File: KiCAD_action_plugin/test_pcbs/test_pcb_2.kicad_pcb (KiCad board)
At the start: 2 copper layers, 36.6 x 26.5 mm, 6 parts

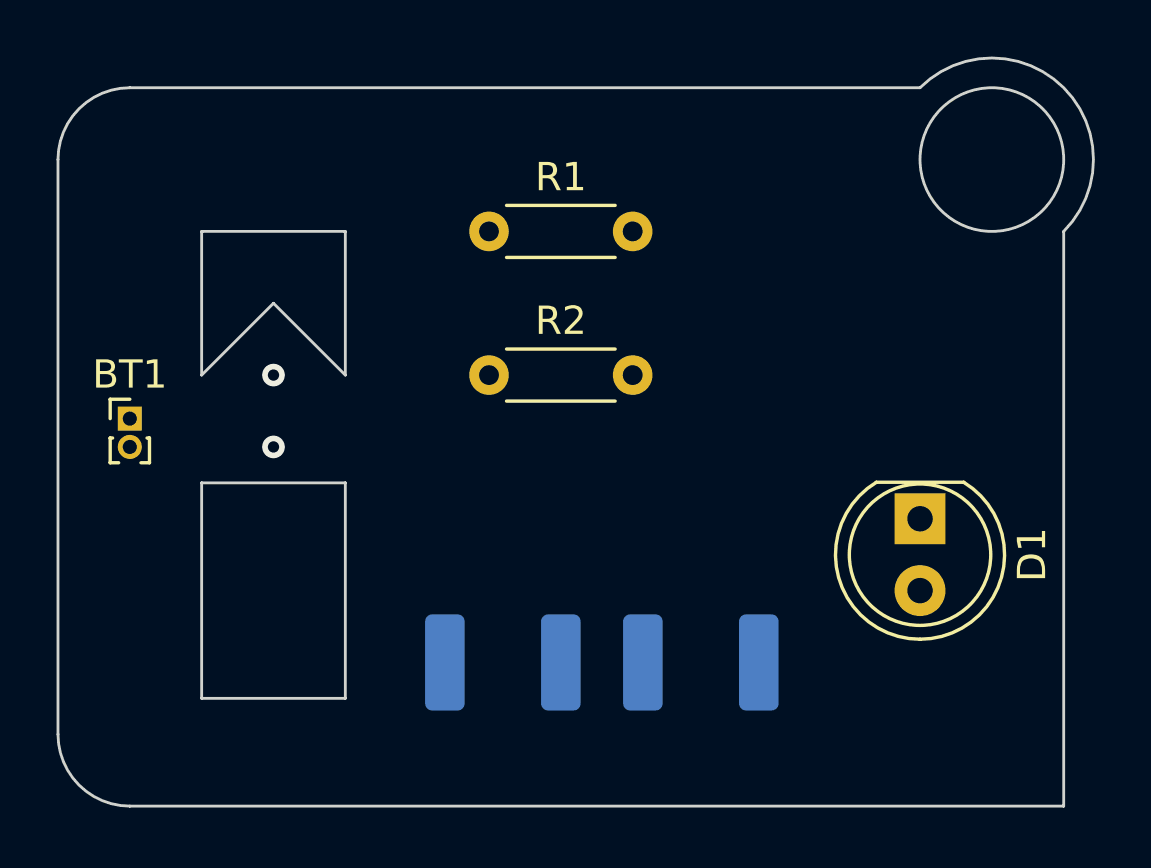
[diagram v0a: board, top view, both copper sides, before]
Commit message: Fix bug when connection couldn't be made after connect->disconnect->connect sequence
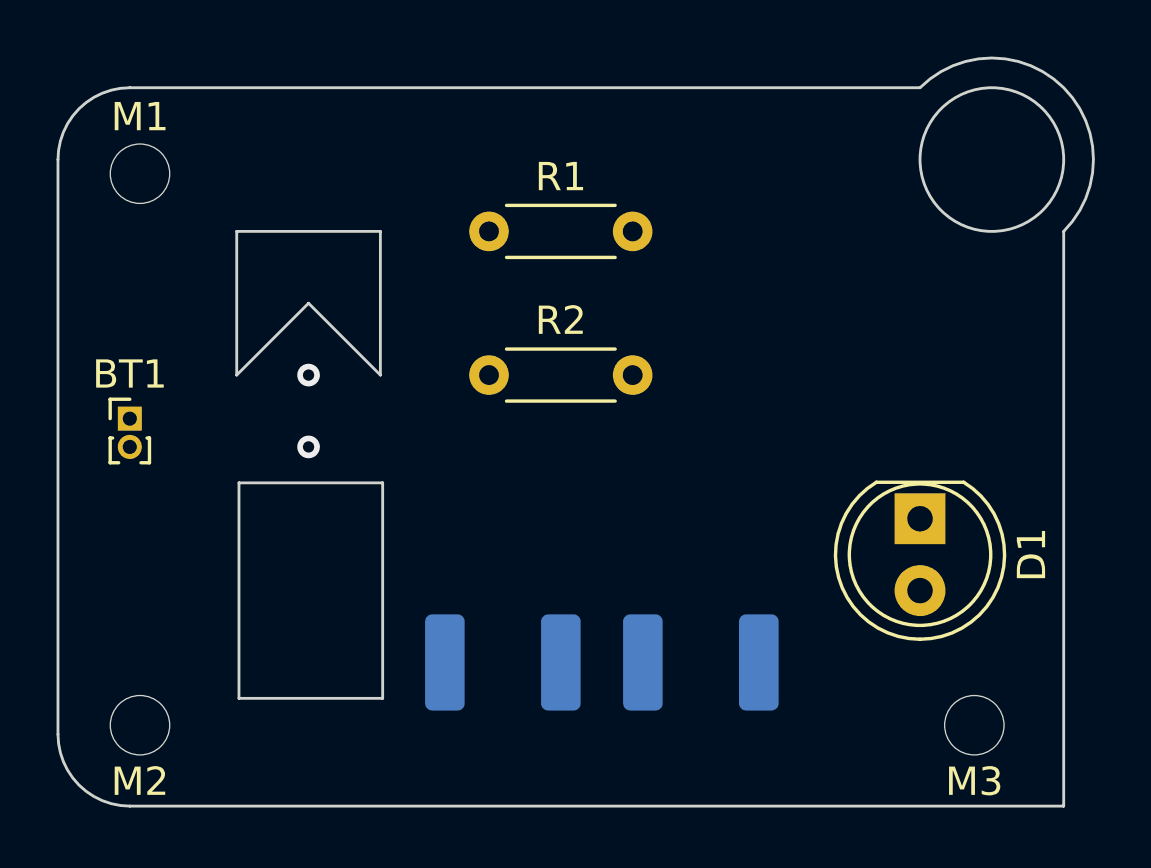
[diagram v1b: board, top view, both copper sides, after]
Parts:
- added M1: MountingHole_2.1mm, MountingHole:MountingHole_2.1mm, F.Cu at (104.5, 64.0)
- added M2: MountingHole_2.1mm, MountingHole:MountingHole_2.1mm, F.Cu at (104.5, 83.5)
- added M3: MountingHole_2.1mm, MountingHole:MountingHole_2.1mm, F.Cu at (134.0, 83.5)
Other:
- outline, holes or cut-outs redrawn
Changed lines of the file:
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@@
   (net 5 "Net-(BT1--)")
   (net 6 "Net-(R3-Pad2)")
+  (footprint "MountingHole:MountingHole_2.1mm" (layer "F.Cu")
+    (at 134 83.5)
+    (descr "Mounting Hole 2.1mm, no annular")
+    (tags "mounting hole 2.1mm no annular")
+    (attr exclude_from_pos_files exclude_from_bom)
+    (fp_text reference "M3" (at 0 2) (layer "F.SilkS")
+        (effects (font (size 1 1) (thickness 0.15)))
+    )
+    (fp_text value "MountingHole_2.1mm" (at 0 3.2) (layer "F.Fab")
+        (effects (font (size 1 1) (thickness 0.15)))
+    )
+    (fp_text user "${REFERENCE}" (at 0 0) (layer "F.Fab")
+        (effects (font (size 1 1) (thickness 0.15)))
+    )
+    (fp_circle (center 0 0) (end 2.1 0)
+      (stroke (width 0.15) (type solid)) (fill none) (layer "Cmts.User"))
+    (fp_circle (center 0 0) (end 2.35 0)
+      (stroke (width 0.05) (type solid)) (fill none) (layer "F.CrtYd"))
+    (pad "" np_thru_hole circle (at 0 0) (size 2.1 2.1) (drill 2.1) (layers "*.Cu" "*.Mask"))
+  )
+  (footprint "MountingHole:MountingHole_2.1mm" (layer "F.Cu")
+    (at 104.5 64)
+    (descr "Mounting Hole 2.1mm, no annular")
+    (tags "mounting hole 2.1mm no annular")
+    (attr exclude_from_pos_files exclude_from_bom)
+    (fp_text reference "M1" (at 0 -2) (layer "F.SilkS")
+        (effects (font (size 1 1) (thickness 0.15)))
+    )
+    (fp_text value "MountingHole_2.1mm" (at 0 3.2) (layer "F.Fab")
+        (effects (font (size 1 1) (thickness 0.15)))
+    )
+    (fp_text user "${REFERENCE}" (at 0 0) (layer "F.Fab")
+        (effects (font (size 1 1) (thickness 0.15)))
+    )
+    (fp_circle (center 0 0) (end 2.1 0)
+      (stroke (width 0.15) (type solid)) (fill none) (layer "Cmts.User"))
+    (fp_circle (center 0 0) (end 2.35 0)
+      (stroke (width 0.05) (type solid)) (fill none) (layer "F.CrtYd"))
+    (pad "" np_thru_hole circle (at 0 0) (size 2.1 2.1) (drill 2.1) (layers "*.Cu" "*.Mask"))
+  )
+  (footprint "MountingHole:MountingHole_2.1mm" (layer "F.Cu")
+    (at 104.5 83.5)
+    (descr "Mounting Hole 2.1mm, no annular")
+    (tags "mounting hole 2.1mm no annular")
+    (attr exclude_from_pos_files exclude_from_bom)
+    (fp_text reference "M2" (at 0 2) (layer "F.SilkS")
+        (effects (font (size 1 1) (thickness 0.15)))
+    )
+    (fp_text value "MountingHole_2.1mm" (at 0 3.2) (layer "F.Fab")
+        (effects (font (size 1 1) (thickness 0.15)))
+    )
+    (fp_text user "${REFERENCE}" (at 0 0) (layer "F.Fab")
+        (effects (font (size 1 1) (thickness 0.15)))
+    )
+    (fp_circle (center 0 0) (end 2.1 0)
+      (stroke (width 0.15) (type solid)) (fill none) (layer "Cmts.User"))
+    (fp_circle (center 0 0) (end 2.35 0)
+      (stroke (width 0.05) (type solid)) (fill none) (layer "F.CrtYd"))
+    (pad "" np_thru_hole circle (at 0 0) (size 2.1 2.1) (drill 2.1) (layers "*.Cu" "*.Mask"))
+  )
   (footprint "Resistor_THT:R_Axial_DIN0204_L3.6mm_D1.6mm_P5.08mm_Horizontal" (layer "F.Cu")
     (at 116.84 71.12)
@@
   (gr_line (start 101.6 63.5) (end 101.6 83.82)
     (stroke (width 0.1) (type default)) (layer "Edge.Cuts"))
-  (gr_rect (start 106.68 74.93) (end 111.76 82.55)
+  (gr_rect (start 108 74.93) (end 113.08 82.55)
     (stroke (width 0.1) (type default)) (fill none) (layer "Edge.Cuts"))
   (gr_poly
     (pts
-      (xy 106.68 71.12)
-      (xy 109.22 68.58)
-      (xy 111.76 71.12)
-      (xy 111.76 66.04)
-      (xy 106.68 66.04)
+      (xy 107.92 71.12)
+      (xy 110.46 68.58)
+      (xy 113 71.12)
+      (xy 113 66.04)
+      (xy 107.92 66.04)
     )
     (stroke (width 0.1) (type solid)) (fill none) (layer "Edge.Cuts"))
@@
   (gr_arc (start 101.6 63.5) (mid 102.343949 61.703949) (end 104.14 60.96)
     (stroke (width 0.1) (type default)) (layer "Edge.Cuts"))
-  (via (at 109.22 73.66) (size 0.8) (drill 0.4) (layers "F.Cu" "B.Cu") (net 0))
-  (via (at 109.22 71.12) (size 0.8) (drill 0.4) (layers "F.Cu" "B.Cu") (net 0))
+  (via (at 110.46 73.66) (size 0.8) (drill 0.4) (layers "F.Cu" "B.Cu") (net 0))
+  (via (at 110.46 71.12) (size 0.8) (drill 0.4) (layers "F.Cu" "B.Cu") (net 0))
 )
